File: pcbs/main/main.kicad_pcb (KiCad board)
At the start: 2 copper layers, 114 x 123.3 mm, 64 parts, among them J1 JST_XH_B3B, J2 Jumpers, J3 JST_XH_B3B, J4 XT30PW-M, Q1 2SC945, Q2 2SC945, Q3 2SC945, Q4 2SC945, Q5 2SC945, Q6 2SC945, Q7 2SC945, Q8 2SC945, U1 ESP32-DEVKITC-32U, U2 AMS1117-3.3

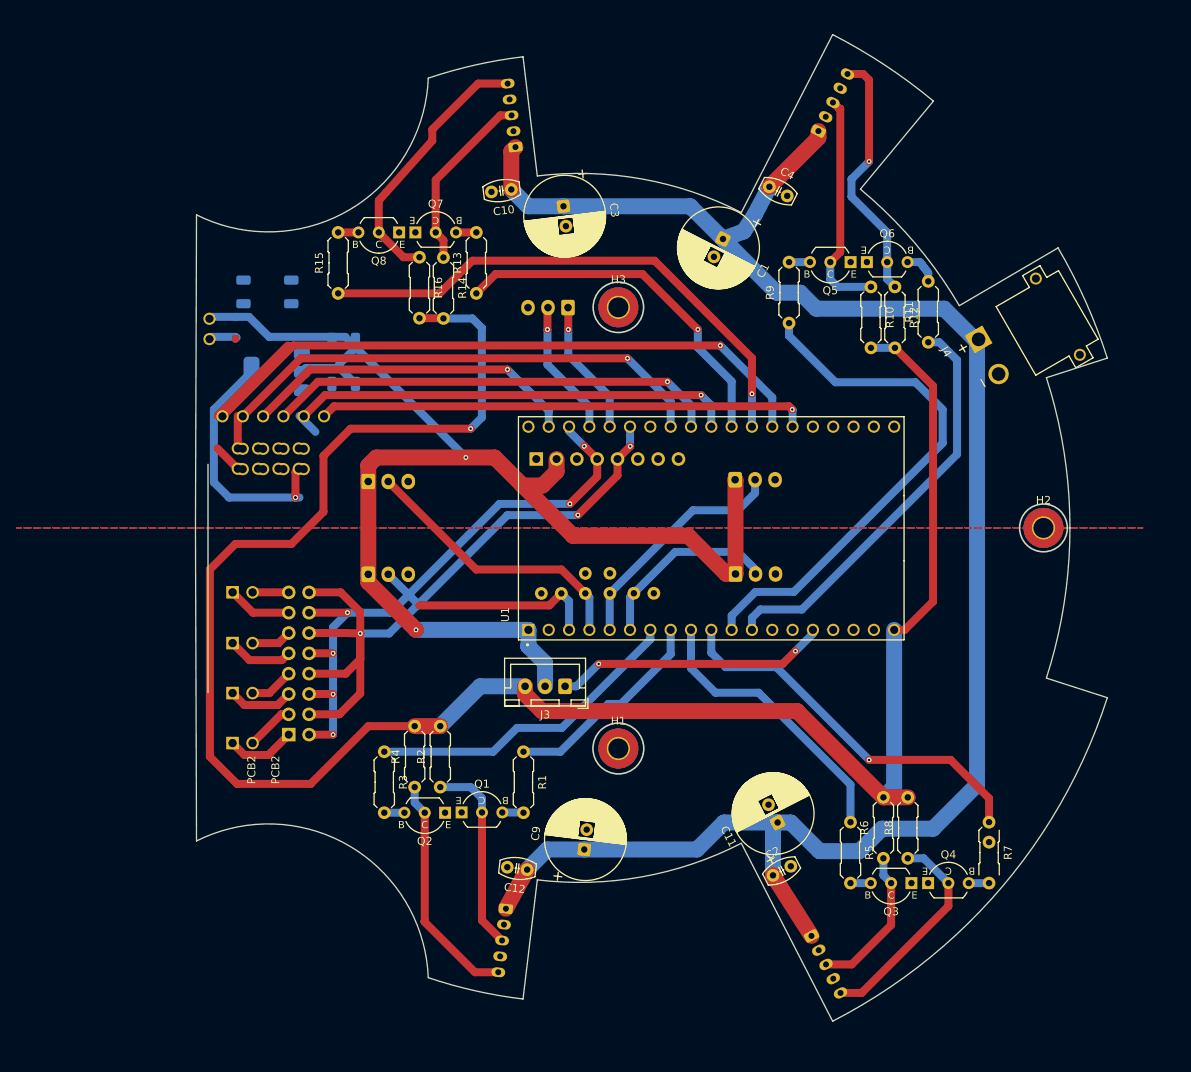
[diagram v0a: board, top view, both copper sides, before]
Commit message: Revert "Merge branch 'main' into add_motor_fb"
This reverts commit ce4cdcf7923af6dec951cf60c694d388183d0360, reversing
changes made to 437a8598f38fb1ac3a6e5ead924260d23a6ed5a3.
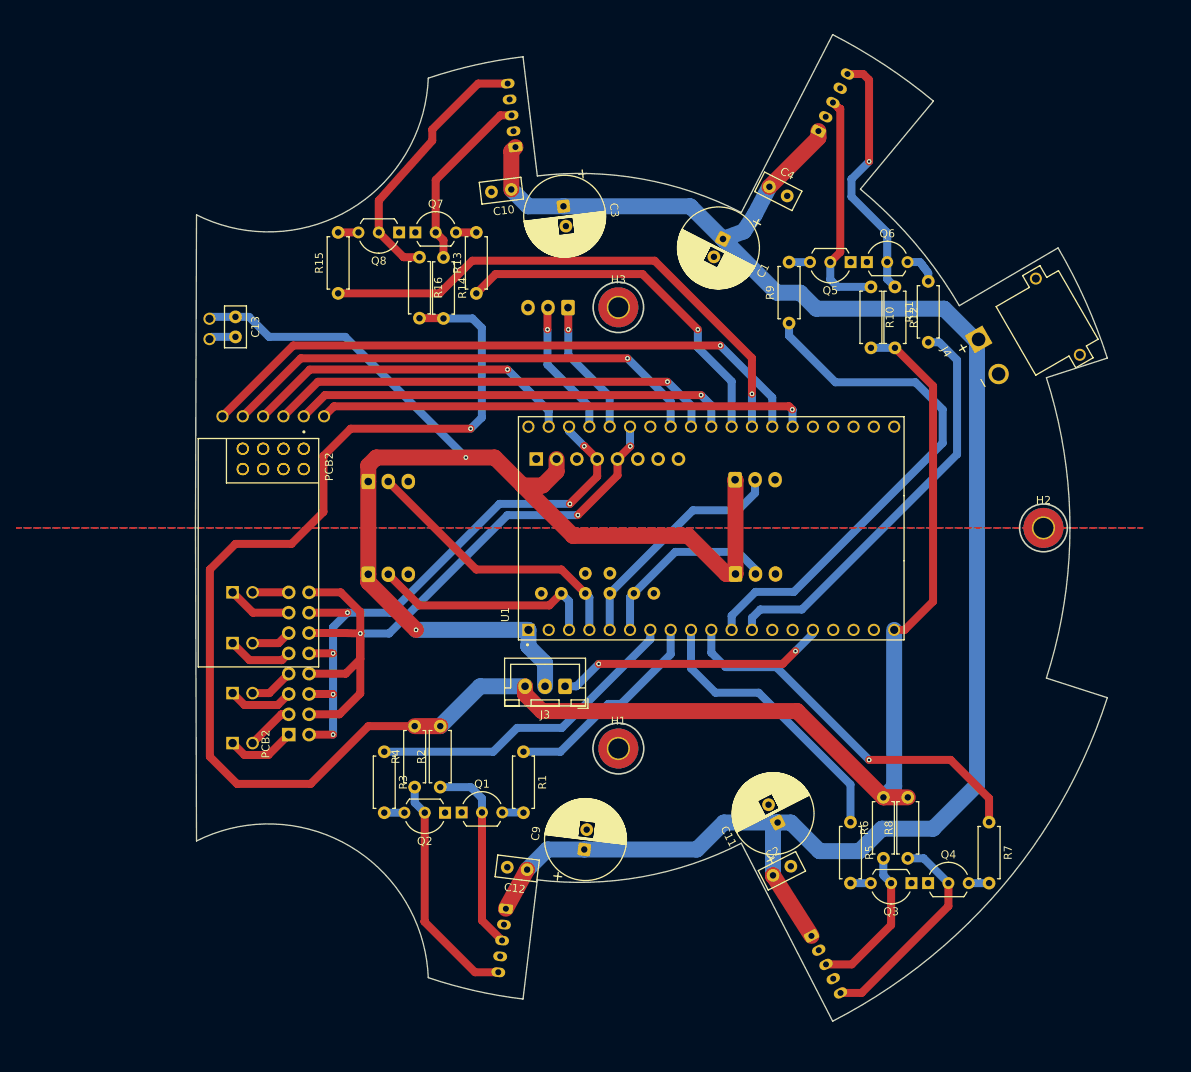
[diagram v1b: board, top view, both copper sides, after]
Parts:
- removed C14, C15, C16: 10uF, Capacitor_SMD:C_1206_3216Metric
- removed U2: AMS1117-3.3, Package_TO_SOT_SMD:SOT-223-3_TabPin2
- C10, C12, C2, C4, C5, C6, C7, C8: footprint PCM_Capacitor_THT_AKL:C_Disc_D5.0mm_W2.5mm_P2.50mm -> Capacitor_THT:C_Disc_D5.0mm_W2.5mm_P2.50mm
- C13: value 10uF -> 100 nF; footprint Capacitor_SMD:C_1206_3216Metric -> Capacitor_THT:C_Disc_D5.0mm_W2.5mm_P2.50mm; moved to F.Cu
- Q1, Q2, Q3, Q4, Q5, Q6, Q7, Q8: footprint PCM_Package_TO_SOT_THT_AKL:TO-92_Inline_Wide_ECB -> Package_TO_SOT_THT:TO-92L_Inline_Wide
- R1, R10, R11, R12, R13, R14, R15, R2, R3, R4, R5, R6, R7, R8, R9: footprint PCM_Resistor_THT_AKL:R_Axial_DIN0207_L6.3mm_D2.5mm_P7.62mm_Horizontal -> Resistor_THT:R_Axial_DIN0207_L6.3mm_D2.5mm_P7.62mm_Horizontal
- moved PCB2 3.45 mm to (74.9, 100.4)
- moved C13 3.28 mm to (72.0, 68.6), turned to -90 degrees
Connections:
- C13 pad 1: +5V -> +3.3V
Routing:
- net 71: track 43.1 -> 0.00 mm, vias 2 -> 0
- net 59: track 16.0 -> 0.00 mm
- net 36: track 8.33 -> 0.00 mm
- net /esp32/M1_ENC: track 27.4 -> 28.8 mm

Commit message: Final rev. V02 main board
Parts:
- removed C2: 100 nF, Capacitor_THT:C_Disc_D5.0mm_W2.5mm_P2.50mm
- removed J4: XT30PW-M, Oxebots:AMASS_XT30PW-M
- removed as1: M1_ENC_I2C, Oxebots:JST_B2B-XH-A
- removed as2: M2_ENC_I2C, Oxebots:JST_B2B-XH-A
- removed as3: M3_ENC_I2C, Oxebots:JST_B2B-XH-A
- removed as4: M4_ENC_I2C, Oxebots:JST_B2B-XH-A
- removed as5600_1: M1_ENC_AN, Connector_JST:JST_XH_B3B-XH-A_1x03_P2.50mm_Vertical
- removed as5600_2: M2_ENC_AN, Connector_JST:JST_XH_B3B-XH-A_1x03_P2.50mm_Vertical
- removed as5600_3: M3_ENC_AN, Connector_JST:JST_XH_B3B-XH-A_1x03_P2.50mm_Vertical
- removed as5600_4: M4_ENC_AN, Connector_JST:JST_XH_B3B-XH-A_1x03_P2.50mm_Vertical
- added C14: 47uF, Capacitor_THT:CP_Radial_D10.0mm_P2.50mm, F.Cu at (129.9, 60.3)
- added C15: 100 nF, Capacitor_SMD:C_0603_1608Metric, B.Cu at (144.1, 47.6)
- added C16: 47uF, Capacitor_THT:CP_Radial_D10.0mm_P2.50mm, F.Cu at (132.3, 128.2)
- added C17: 100 nF, Capacitor_SMD:C_0603_1608Metric, B.Cu at (142.9, 141.7)
- added C18: 47uF, Capacitor_THT:CP_Radial_D10.0mm_P2.50mm, F.Cu at (110.3, 131.9)
- added C19: 100 nF, Capacitor_SMD:C_0603_1608Metric, B.Cu at (105.4, 139.2)
- added D1: LED, LED_SMD:LED_0603_1608Metric, B.Cu at (71.0, 59.4)
- added D10: BAT54S, Package_TO_SOT_SMD:SOT-23, B.Cu at (153.7, 43.2)
- added D11: BAT54S, Package_TO_SOT_SMD:SOT-23, B.Cu at (153.9, 147.3)
- added D12: BAT54S, Package_TO_SOT_SMD:SOT-23, B.Cu at (99.1, 147.0)
- added D13: LED, LED_SMD:LED_0603_1608Metric, B.Cu at (121.8, 71.8)
- added D14: LED, LED_SMD:LED_0603_1608Metric, B.Cu at (121.8, 73.7)
- added D15: LED, LED_SMD:LED_0603_1608Metric, B.Cu at (121.8, 75.6)
- added D16: LED, LED_SMD:LED_0603_1608Metric, B.Cu at (121.8, 77.5)
- added D2: LED, LED_SMD:LED_0603_1608Metric, B.Cu at (78.1, 92.7)
- added D3: LED, LED_SMD:LED_0603_1608Metric, B.Cu at (76.2, 107.2)
- added D4: LED, LED_SMD:LED_0603_1608Metric, B.Cu at (80.0, 107.2)
- added D5: LED, LED_SMD:LED_0603_1608Metric, B.Cu at (95.0, 133.3)
- added D6: LED, LED_SMD:LED_0603_1608Metric, B.Cu at (158.1, 136.0)
- added D7: LED, LED_SMD:LED_0603_1608Metric, B.Cu at (150.1, 59.4)
- added D8: LED, LED_SMD:LED_0603_1608Metric, B.Cu at (94.6, 50.8)
- added D9: BAT54S, Package_TO_SOT_SMD:SOT-23, B.Cu at (98.3, 42.5)
- added R17: 10k, Resistor_SMD:R_0603_1608Metric, B.Cu at (148.6, 54.8)
- added R18: 10k, Resistor_SMD:R_0603_1608Metric, B.Cu at (149.1, 43.5)
- added R19: 20k, Resistor_SMD:R_0603_1608Metric, B.Cu at (150.5, 40.6)
- added R20: 10k, Resistor_SMD:R_0603_1608Metric, B.Cu at (144.8, 63.0)
- added R21: 10k, Resistor_SMD:R_0603_1608Metric, B.Cu at (147.3, 63.0)
- added R22: 47k, Resistor_SMD:R_0603_1608Metric, B.Cu at (144.1, 57.1)
- added R23: 10k, Resistor_SMD:R_0603_1608Metric, B.Cu at (150.1, 62.5)
- added R24: 10k, Resistor_SMD:R_0603_1608Metric, B.Cu at (156.2, 133.0)
- added R25: 10k, Resistor_SMD:R_0603_1608Metric, B.Cu at (149.4, 146.3)
- added R26: 20k, Resistor_SMD:R_0603_1608Metric, B.Cu at (150.9, 149.4)
- added R27: 10k, Resistor_SMD:R_0603_1608Metric, B.Cu at (153.7, 133.0)
- added R28: 10k, Resistor_SMD:R_0603_1608Metric, B.Cu at (151.8, 133.0)
- added R29: 47k, Resistor_SMD:R_0603_1608Metric, B.Cu at (152.4, 139.1)
- added R30: 10k, Resistor_SMD:R_0603_1608Metric, B.Cu at (151.1, 141.4)
- added R31: 10k, Resistor_SMD:R_0603_1608Metric, B.Cu at (96.0, 139.9)
- added R32: 10k, Resistor_SMD:R_0603_1608Metric, B.Cu at (102.6, 144.8)
- added R33: 20k, Resistor_SMD:R_0603_1608Metric, B.Cu at (102.1, 148.3)
- added R34: 10k, Resistor_SMD:R_0603_1608Metric, B.Cu at (96.5, 131.4)
- added R35: 10k, Resistor_SMD:R_0603_1608Metric, B.Cu at (98.0, 131.4)
- added R36: 47k, Resistor_SMD:R_0603_1608Metric, B.Cu at (101.6, 136.5)
- added R37: 10k, Resistor_SMD:R_0603_1608Metric, B.Cu at (100.6, 131.4)
- added R38: 220, Resistor_SMD:R_0603_1608Metric, B.Cu at (118.7, 71.8)
- added R39: 220, Resistor_SMD:R_0603_1608Metric, B.Cu at (118.7, 73.7)
- added R40: 220, Resistor_SMD:R_0603_1608Metric, B.Cu at (118.7, 75.6)
- added R41: 220, Resistor_SMD:R_0603_1608Metric, B.Cu at (118.7, 77.5)
- added TP1: 24V probe, TestPoint:TestPoint_Pad_D1.0mm, B.Cu at (126.1, 77.5)
- added TP10: M1_FB_Probe, TestPoint:TestPoint_Loop_D2.50mm_Drill1.0mm_LowProfile, B.Cu at (89.5, 55.2)
- added TP11: V_{mon} probe, TestPoint:TestPoint_Pad_D1.0mm, B.Cu at (124.6, 79.2)
- added TP12: M1_PWM_Probe, TestPoint:TestPoint_Loop_D2.50mm_Drill1.0mm_LowProfile, B.Cu at (89.7, 61.3)
- added TP13: M2_{ENC} probe, TestPoint:TestPoint_Loop_D2.50mm_Drill1.0mm_LowProfile, B.Cu at (133.3, 107.3)
- added TP14: M3_{ENC} probe, TestPoint:TestPoint_Loop_D2.50mm_Drill1.0mm_LowProfile, B.Cu at (130.8, 109.9)
- added TP15: M4_{ENC} probe, TestPoint:TestPoint_Loop_D2.50mm_Drill1.0mm_LowProfile, B.Cu at (133.3, 112.4)
- added TP16: M1_{ENC} probe, TestPoint:TestPoint_Loop_D2.50mm_Drill1.0mm_LowProfile, B.Cu at (130.8, 114.9)
- added TP17: G_{INT} probe, TestPoint:TestPoint_Loop_D2.50mm_Drill1.0mm_LowProfile, B.Cu at (69.1, 107.1)
- added TP18: M4_FB_Probe, TestPoint:TestPoint_Loop_D2.50mm_Drill1.0mm_LowProfile, B.Cu at (92.8, 128.7)
- added TP19: CSN_{RF24} probe, TestPoint:TestPoint_Loop_D2.50mm_Drill1.0mm_LowProfile, B.Cu at (86.2, 57.4)
- added TP2: 12V probe, TestPoint:TestPoint_Pad_D1.0mm, B.Cu at (125.3, 75.6)
- added TP20: IRQ_{RF24} probe, TestPoint:TestPoint_Loop_D2.50mm_Drill1.0mm_LowProfile, B.Cu at (82.5, 59.9)
- added TP21: M_{RDY} probe, TestPoint:TestPoint_Loop_D2.50mm_Drill1.0mm_LowProfile, B.Cu at (69.1, 99.6)
- added TP22: SR_LATCH probe, TestPoint:TestPoint_Loop_D2.50mm_Drill1.0mm_LowProfile, B.Cu at (165.7, 94.6)
- added TP23: A_{INT1} probe, TestPoint:TestPoint_Loop_D2.50mm_Drill1.0mm_LowProfile, B.Cu at (69.1, 103.4)
- added TP24: CLK_{SPI} probe, TestPoint:TestPoint_Loop_D2.50mm_Drill1.0mm_LowProfile, B.Cu at (165.7, 99.8)
- added TP25: MISO_{SPI} probe, TestPoint:TestPoint_Loop_D2.50mm_Drill1.0mm_LowProfile, B.Cu at (165.7, 103.5)
- added TP26: SDA_{I2C}, TestPoint:TestPoint_Loop_D2.50mm_Drill1.0mm_LowProfile, B.Cu at (165.7, 107.3)
- added TP27: INT_{TOF}, TestPoint:TestPoint_Loop_D2.50mm_Drill1.0mm_LowProfile, B.Cu at (168.9, 134.6)
- added TP28: SCL_{I2C}, TestPoint:TestPoint_Loop_D2.50mm_Drill1.0mm_LowProfile, B.Cu at (165.7, 114.9)
- added TP29: MOSI_{SPI} probe, TestPoint:TestPoint_Loop_D2.50mm_Drill1.0mm_LowProfile, B.Cu at (159.4, 123.8)
- added TP3: 3.3V probe, TestPoint:TestPoint_Pad_D1.0mm, B.Cu at (125.3, 71.8)
- added TP4: 5V probe, TestPoint:TestPoint_Pad_D1.0mm, B.Cu at (126.1, 73.7)
- added TP5: M3_FB_Probe, TestPoint:TestPoint_Loop_D2.50mm_Drill1.0mm_LowProfile, B.Cu at (160.0, 142.9)
- added TP6: M4_PWM_Probe, TestPoint:TestPoint_Loop_D2.50mm_Drill1.0mm_LowProfile, B.Cu at (103.6, 128.8)
- added TP7: M3_PWM_Probe, TestPoint:TestPoint_Loop_D2.50mm_Drill1.0mm_LowProfile, B.Cu at (147.8, 141.2)
- added TP8: M2_FB_Probe, TestPoint:TestPoint_Loop_D2.50mm_Drill1.0mm_LowProfile, B.Cu at (152.0, 46.3)
- added TP9: M2_PWM_Probe, TestPoint:TestPoint_Loop_D2.50mm_Drill1.0mm_LowProfile, B.Cu at (150.1, 65.9)
- added U3: ESP32-DEVKITC-32U, Oxebots:MODULE_ESP32-DEVKITC-32U, B.Cu at (149.4, 97.3)
- added U4: AMS1117-3.3, Package_TO_SOT_SMD:SOT-223-3_TabPin2, B.Cu at (75.8, 75.5)
- added U5: 4052, Package_DIP:DIP-16_W7.62mm, F.Cu at (92.7, 95.9)
- C1, C11, C3, C9: value 47uF -> 100 nF; footprint Capacitor_THT:CP_Radial_D10.0mm_P2.50mm -> Capacitor_SMD:C_0603_1608Metric; moved to B.Cu
- C10, C12, C13: footprint Capacitor_THT:C_Disc_D5.0mm_W2.5mm_P2.50mm -> Capacitor_SMD:C_0603_1608Metric; moved to B.Cu
- C4: value 100 nF -> 10 uF; footprint Capacitor_THT:C_Disc_D5.0mm_W2.5mm_P2.50mm -> Capacitor_SMD:C_0805_2012Metric; moved to B.Cu
- C5, C6, C7: value 100 nF -> 10 uF; footprint Capacitor_THT:C_Disc_D5.0mm_W2.5mm_P2.50mm -> Capacitor_SMD:C_0805_2012Metric
- C8: value 100 nF -> 47uF; footprint Capacitor_THT:C_Disc_D5.0mm_W2.5mm_P2.50mm -> Capacitor_THT:CP_Radial_D10.0mm_P2.50mm; moved to F.Cu
- J1: value JST_XH_B3B -> PB_IDC_16_PIN; footprint Connector_JST:JST_XH_B3B-XH-A_1x03_P2.50mm_Vertical -> Connector_IDC:IDC-Header_2x08_P2.54mm_Vertical
- J2: value Jumpers -> KICKER_IDC_16_PIN; footprint Connector_PinHeader_2.54mm:PinHeader_2x08_P2.54mm_Vertical -> Connector_IDC:IDC-Header_2x08_P2.54mm_Vertical; moved to F.Cu
- J3: value JST_XH_B3B -> ENC_IDC_16_PIN; footprint Connector_JST:JST_XH_B3B-XH-A_1x03_P2.50mm_Vertical -> Connector_IDC:IDC-Header_2x08_P2.54mm_Vertical
- M1: value ~ -> FRONT_LEFT_MOTOR
- M2: value ~ -> BACK_LEFT_MOTOR
- M3: value ~ -> BACK_RIGHT_MOTOR
- M4: value ~ -> FRONT_RIGHT_MOTOR
- PCB1: value ~ -> VL53L5CX; footprint Oxebots:NRF24L01_PWR_ADP -> Connector_JST:JST_XH_B6B-XH-A_1x06_P2.50mm_Vertical; moved to F.Cu
- PCB2: value ~ -> NRF24L01; moved to B.Cu
- Q1, Q2, Q3, Q4, Q5, Q6, Q7, Q8: footprint Package_TO_SOT_THT:TO-92L_Inline_Wide -> Package_TO_SOT_THT:TO-92
- R1, R2, R3, R4, R5, R6, R7, R8: value 10k -> 220; footprint Resistor_THT:R_Axial_DIN0207_L6.3mm_D2.5mm_P7.62mm_Horizontal -> Resistor_SMD:R_0603_1608Metric; moved to B.Cu
- R10, R11, R13, R14, R16, R9: footprint Resistor_THT:R_Axial_DIN0207_L6.3mm_D2.5mm_P7.62mm_Horizontal -> Resistor_SMD:R_0603_1608Metric; moved to B.Cu
- R12: value 10k -> 20k; footprint Resistor_THT:R_Axial_DIN0207_L6.3mm_D2.5mm_P7.62mm_Horizontal -> Resistor_SMD:R_0603_1608Metric; moved to B.Cu
- R15: value 10k -> 47k; footprint Resistor_THT:R_Axial_DIN0207_L6.3mm_D2.5mm_P7.62mm_Horizontal -> Resistor_SMD:R_0603_1608Metric; moved to B.Cu
- U1: value ESP32-DEVKITC-32U -> 74HC595; footprint Oxebots:MODULE_ESP32-DEVKITC-32U -> Package_DIP:DIP-16_W7.62mm
- moved PCB1 105.4 mm to (174.0, 117.3), turned to -108 degrees
- moved R8 102.9 mm to (92.6, 55.3)
- moved M2 101.8 mm to (144.9, 44.2), turned to 63 degrees
- moved M3 100.1 mm to (144.0, 145.5), turned to -63 degrees
- moved M4 95.7 mm to (105.8, 143.1), turned to -96.8 degrees
- moved M1 95.6 mm to (106.6, 47.1), turned to 97 degrees
- moved C1 91.0 mm to (71.8, 126.2), turned to -90 degrees
- moved Q3 86.5 mm to (147.3, 53.3)
- moved C9 84.1 mm to (107.5, 51.5), turned to -173 degrees
- moved C3 83.4 mm to (170.8, 114.9), turned to -108 degrees
- moved Q7 81.9 mm to (98.1, 139.9)
- moved Q4 81.0 mm to (144.8, 59.6)
- moved Q6 79.4 mm to (153.7, 141.1)
- moved Q2 78.2 mm to (98.6, 52.4)
- moved R7 77.1 mm to (150.1, 56.4)
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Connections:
- C1 pad 1: +24V -> GND
- C1 pad 2: GND -> +3.3V
- C10 pad 1: +24V -> ENC_{M1}
- C11 pad 1: +24V -> ENC_{M2}
- C12 pad 1: +24V -> ENC_{M3}
- C13 pad 1: +3.3V -> ENC_{M4}
- C3 pad 1: +24V -> GND
- C3 pad 2: GND -> +3.3V
- C4 pad 1: +24V -> GND
- C4 pad 2: GND -> +5V
- C5 pad 1: /esp32/M1_ENC -> GND
- C5 pad 2: GND -> +5V
- C6 pad 1: /esp32/M2_ENC -> GND
- C6 pad 2: GND -> +3.3V
- C7 pad 1: /esp32/M3_ENC -> GND
- C7 pad 2: GND -> +3.3V
- C8 pad 1: /esp32/M4_ENC -> +24V
- IMU1 pad 4: /esp32/I2C.SCL -> SCL_{I2C}
- IMU1 pad 5: /esp32/I2C.SDA -> SDA_{I2C}
- IMU1 pad 6: unconnected-(IMU1-Pin_6-Pad6) -> M_{DRDY}
- IMU1 pad 7: unconnected-(IMU1-Pin_7-Pad7) -> A_{INT1}
- IMU1 pad 8: unconnected-(IMU1-Pin_8-Pad8) -> G_{INT}
- J1 pad 1: /esp32/KICKER_EN -> +24V
- J1 pad 2: /esp32/KICKER_PWM -> +24V
- J1 pad 3: unconnected-(J1-Pin_3-Pad3) -> +24V
- J2 pad 1: Net-(J2-Pin_1) -> +24V
- J2 pad 10: /esp32/I2C.SCL -> SCL_{I2C}
- J2 pad 11: Net-(J2-Pin_11) -> GND
- J2 pad 12: /esp32/I2C.SDA -> GND
- J2 pad 13: Net-(J2-Pin_13) -> GND
- J2 pad 14: /esp32/I2C.SCL -> GND
- J2 pad 15: Net-(J2-Pin_15) -> GND
- J2 pad 16: /esp32/I2C.SDA -> GND
- J2 pad 2: /esp32/I2C.SCL -> +24V
- J2 pad 3: Net-(J2-Pin_3) -> +24V
- J2 pad 4: /esp32/I2C.SDA -> +24V
- J2 pad 5: Net-(J2-Pin_5) -> +24V
- J2 pad 6: /esp32/I2C.SCL -> +24V
- J2 pad 7: Net-(J2-Pin_7) -> +12V
- J2 pad 8: /esp32/I2C.SDA -> SDA_{I2C}
- J2 pad 9: Net-(J2-Pin_9) -> +3.3V
- J3 pad 1: /esp32/V_{MON} -> /motors/SDA_{M4_ENC}
- J3 pad 3: +5V -> /motors/SCL_{M4_ENC}
- M1 pad 2: unconnected-(M1-Feedback-Pad2) -> Net-(M1-Feedback)
- M2 pad 2: unconnected-(M2-Feedback-Pad2) -> Net-(M2-Feedback)
- M3 pad 2: unconnected-(M3-Feedback-Pad2) -> Net-(M3-Feedback)
- M4 pad 2: unconnected-(M4-Feedback-Pad2) -> Net-(M4-Feedback)
- PCB1 pad 1: Net-(PCB1-GND_{out}) -> +3.3V
- PCB1 pad 2: Net-(PCB1-CE) -> GND
- PCB1 pad 3: Net-(PCB1-SCK) -> SCL_{I2C}
- PCB1 pad 4: Net-(PCB1-MISO) -> SDA_{I2C}
- PCB1 pad 5: Net-(PCB1-VCC_{out}) -> INT_{TOF}
- PCB1 pad 6: Net-(PCB1-CSN) -> unconnected-(PCB1-LPn-Pad6)
- PCB2 pad 1: Net-(PCB1-GND_{out}) -> GND
- PCB2 pad 2: Net-(PCB1-CE) -> CE_{RF24}
- PCB2 pad 3: Net-(PCB1-SCK) -> CLK_{SPI}
- PCB2 pad 4: Net-(PCB1-MISO) -> MISO_{SPI}
- PCB2 pad 5: Net-(PCB1-VCC_{out}) -> +3.3V
- PCB2 pad 6: Net-(PCB1-CSN) -> CSN_{RF24}
- PCB2 pad 7: Net-(PCB1-MOSI) -> MOSI_{SPI}
- PCB2 pad 8: Net-(PCB1-IRQ) -> IRQ_{RF24}
- Q1 pad 1: GND -> Net-(Q1-B)
- Q1 pad 2: Net-(M1-DIR) -> GND
- Q1 pad 3: Net-(Q1-B) -> Net-(M1-DIR)
- Q2 pad 1: GND -> Net-(Q2-B)
- Q2 pad 2: Net-(M1-PWM) -> GND
- Q2 pad 3: Net-(Q2-B) -> Net-(M1-PWM)
- Q3 pad 1: GND -> Net-(Q3-B)
- Q3 pad 2: Net-(M2-DIR) -> GND
- Q3 pad 3: Net-(Q3-B) -> Net-(M2-DIR)
- Q4 pad 1: GND -> Net-(Q4-B)
- Q4 pad 2: Net-(M2-PWM) -> GND
- Q4 pad 3: Net-(Q4-B) -> Net-(M2-PWM)
- Q5 pad 1: GND -> Net-(Q5-B)
- Q5 pad 2: Net-(M3-DIR) -> GND
- Q5 pad 3: Net-(Q5-B) -> Net-(M3-DIR)
- Q6 pad 1: GND -> Net-(Q6-B)
- Q6 pad 2: Net-(M3-PWM) -> GND
- Q6 pad 3: Net-(Q6-B) -> Net-(M3-PWM)
- Q7 pad 1: GND -> Net-(Q7-B)
- Q7 pad 2: Net-(M4-DIR) -> GND
- Q7 pad 3: Net-(Q7-B) -> Net-(M4-DIR)
- Q8 pad 1: GND -> Net-(Q8-B)
- Q8 pad 2: Net-(M4-PWM) -> GND
- Q8 pad 3: Net-(Q8-B) -> Net-(M4-PWM)
- R1 pad 1: /esp32/M1_DIR -> CE_{RF24}
- R1 pad 2: Net-(Q1-B) -> Net-(D1-A)
- R10 pad 1: Net-(M3-DIR) -> DIR_{M1}
- R10 pad 2: +5V -> Net-(Q1-B)
- R11 pad 1: /esp32/M3_PWM -> FB_{M1}
- R11 pad 2: Net-(Q6-B) -> Net-(M1-Feedback)
- R12 pad 1: Net-(M3-PWM) -> GND
- R12 pad 2: +5V -> FB_{M1}
- R13 pad 1: /esp32/M4_DIR -> Net-(M1-DIR)
- R13 pad 2: Net-(Q7-B) -> +5V
- R14 pad 1: Net-(M4-DIR) -> Net-(M1-PWM)
- R15 pad 1: /esp32/M4_PWM -> Net-(Q2-B)
- R15 pad 2: Net-(Q8-B) -> GND
- R16 pad 1: Net-(M4-PWM) -> PWM_{M1}
- R16 pad 2: +5V -> Net-(Q2-B)
- R2 pad 1: Net-(M1-DIR) -> MUX_{INH}
- R2 pad 2: +5V -> Net-(D2-A)
- R3 pad 1: /esp32/M1_PWM -> MUX_{B}
- R3 pad 2: Net-(Q2-B) -> Net-(D3-A)
- R4 pad 1: Net-(M1-PWM) -> MUX_{A}
- R4 pad 2: +5V -> Net-(D4-A)
- R5 pad 1: /esp32/M2_DIR -> DIR_{M4}
- R5 pad 2: Net-(Q3-B) -> Net-(D5-A)
- R6 pad 1: Net-(M2-DIR) -> DIR_{M3}
- R6 pad 2: +5V -> Net-(D6-A)
- R7 pad 1: /esp32/M2_PWM -> DIR_{M2}
- R7 pad 2: Net-(Q4-B) -> Net-(D7-A)
- R8 pad 1: Net-(M2-PWM) -> DIR_{M1}
- R8 pad 2: +5V -> Net-(D8-A)
- R9 pad 1: /esp32/M3_DIR -> INT_{TOF}
- R9 pad 2: Net-(Q5-B) -> Net-(U3-TXD0)
- U1 pad 1: +3.3V -> DIR_{M2}
- U1 pad 10: /esp32/M2_PWM -> +3.3V
- U1 pad 11: /esp32/M3_DIR -> CLK_{SPI}
- U1 pad 12: /esp32/M3_PWM -> RCK_{SR}
- U1 pad 13: unconnected-(U1-IO12-Pad13) -> GND
- U1 pad 14: GND -> MOSI_{SPI}
- U1 pad 15: /esp32/V_{MON} -> DIR_{M1}
- U1 pad 16: unconnected-(U1-SD2-Pad16) -> +3.3V
- U1 pad 2: unconnected-(U1-EN-Pad2) -> DIR_{M3}
- U1 pad 3: /esp32/M1_ENC -> DIR_{M4}
- U1 pad 4: /esp32/M2_ENC -> MUX_{A}
- U1 pad 5: /esp32/M3_ENC -> MUX_{B}
- U1 pad 6: /esp32/M4_ENC -> MUX_{INH}
- U1 pad 7: /esp32/M1_PWM -> CE_{RF24}
- U1 pad 8: /esp32/M1_DIR -> GND
- U1 pad 9: /esp32/M2_DIR -> unconnected-(U1-QH'-Pad9)
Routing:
- net +3.3V: track 155.1 -> 510.2 mm, vias 2 -> 10
- net SDA_{I2C}: track 0.00 -> 211.4 mm, vias 0 -> 3
- net +24V: track 231.2 -> 35.4 mm, vias 0 -> 6
- net SCL_{I2C}: track 0.00 -> 191.6 mm, vias 0 -> 3
- net MOSI_{SPI}: track 0.00 -> 178.8 mm, vias 0 -> 3
- net G_{INT}: track 0.00 -> 178.2 mm, vias 0 -> 1
- net M_{DRDY}: track 0.00 -> 175.8 mm, vias 0 -> 1
- net FB_{M4}: track 0.00 -> 174.5 mm, vias 0 -> 3
- net CLK_{SPI}: track 0.00 -> 165.6 mm, vias 0 -> 3
- net A_{INT1}: track 0.00 -> 164.9 mm, vias 0 -> 1
- net FB_{M1}: track 0.00 -> 123.3 mm, vias 0 -> 2
- net DIR_{M3}: track 0.00 -> 120.8 mm, vias 0 -> 4
- net MISO_{SPI}: track 0.00 -> 118.9 mm
- net CSN_{RF24}: track 0.00 -> 117.5 mm
- net FB_{M3}: track 0.00 -> 117.0 mm, vias 0 -> 5
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- added copper zone on F.Cu, net +24V
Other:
- outline, holes or cut-outs redrawn
- board text added: "+12V"
- board text added: "+24V"
- board text added: "+3.3V"
- board text added: "+5V"
- board text added: "A_{INT1}"
- board text added: "CLK_{SPI}"
- board text added: "CSN_{RF}"
- board text added: "ENCODERS"
- board text added: "ENC_{M1}"
- board text added: "ENC_{M3}"
- board text added: "ENC_{M4}"
- board text added: "FB_{M1}"
- board text added: "FB_{M2}"
- board text added: "FB_{M3}"
- board text added: "FB_{M4}"
- board text added: "GND"
- board text added: "G_{INT}"
- board text added: "I2C:"
- board text added: "INT_{TOF}"
- board text added: "IRQ_{RF}"
- board text added: "KICKER INTERFACE"
- board text added: "MISO_{SPI}"
- board text added: "MOSI_{SPI}"
- board text added: "MOTORS:"
- board text added: "M_{DRDY}"
- board text added: "NOTES:"
- board text added: "OTHERS:"
- board text added: "POWER BOARD INTERFACE"
- board text added: "PWM_{M1}"
- board text added: "PWM_{M2}"
- board text added: "PWM_{M3}"
- board text added: "PWM_{M4}"
- board text added: "RCK_{SR}"
- board text added: "RF24:"
- board text added: "SCL_{I2C}"
- board text added: "SDA_{I2C}"
- board text added: "SENSORS:"
- board text added: "SPI:"
- board text added: "TOF VL53L5CX"
- board text added: "V_{MON}"

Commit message: Minor modifications on silkscreen for posterior readability
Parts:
- PCB1: moved to B.Cu
- moved C17 2.96 mm to (145.0, 139.7)
- moved C9 1.15 mm to (107.1, 50.4)
- moved C19 0.62 mm to (104.9, 138.8)
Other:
- board text added: "12V"
- board text added: "24V"
- board text added: "3V3"
- board text added: "5V"
- board text added: "DIR_{M1}"
- board text added: "DIR_{M2}"
- board text added: "DIR_{M3}"
- board text added: "DIR_{M4}"
- board text added: "INT"
- board text added: "M1"
- board text added: "M2"
- board text added: "M3"
- board text added: "M4"
- board text added: "X"
- board text removed: "+12V"
- board text removed: "+24V"
- board text removed: "+3.3V"
- board text removed: "+5V"
